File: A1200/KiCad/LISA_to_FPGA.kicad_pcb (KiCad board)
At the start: 2 copper layers, 64 x 37 mm, 28 parts, among them J1 Conn_01x04, J2 Conn_01x40, U1 LM1117-3.3, U2 74LVC162244ADGG, U3 74LVC162244ADGG, U4 LISA, U5 RP2354B

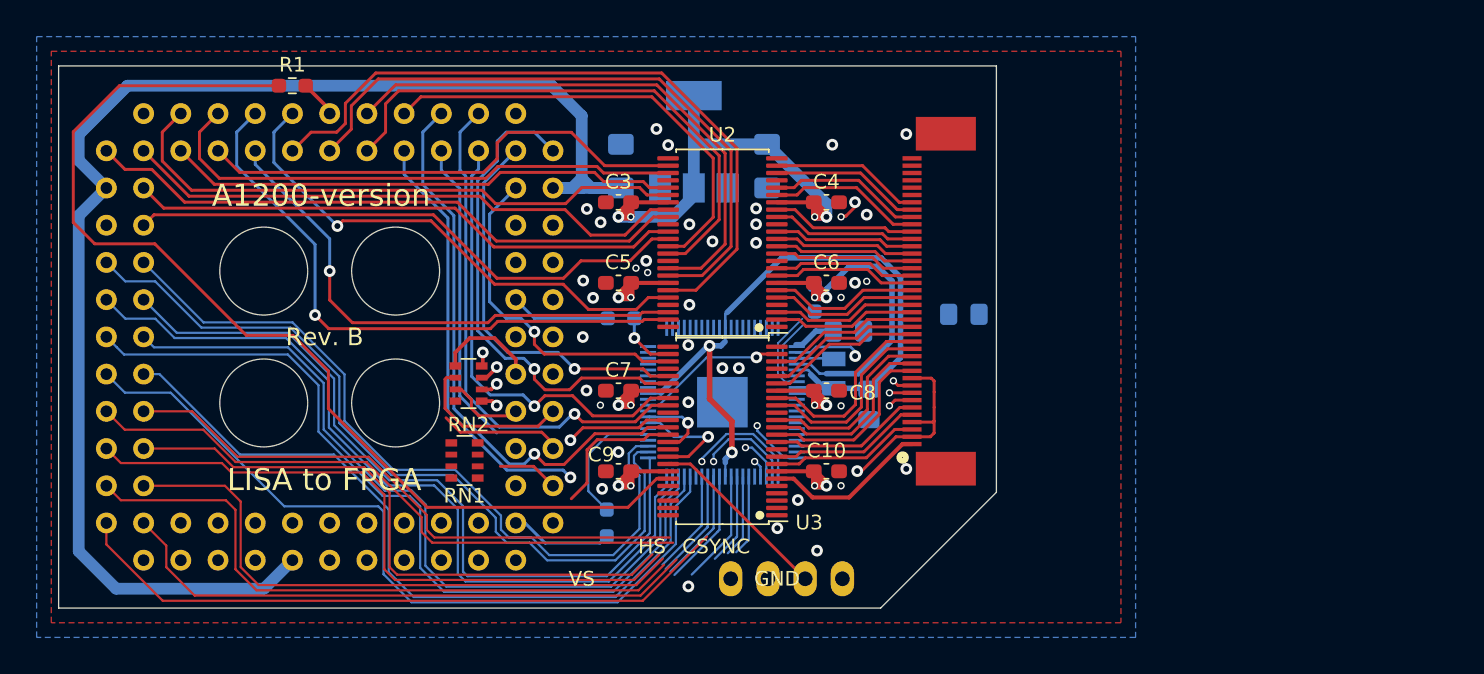
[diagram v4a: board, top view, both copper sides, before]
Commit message: Go to 4 layer and route RGA tracks
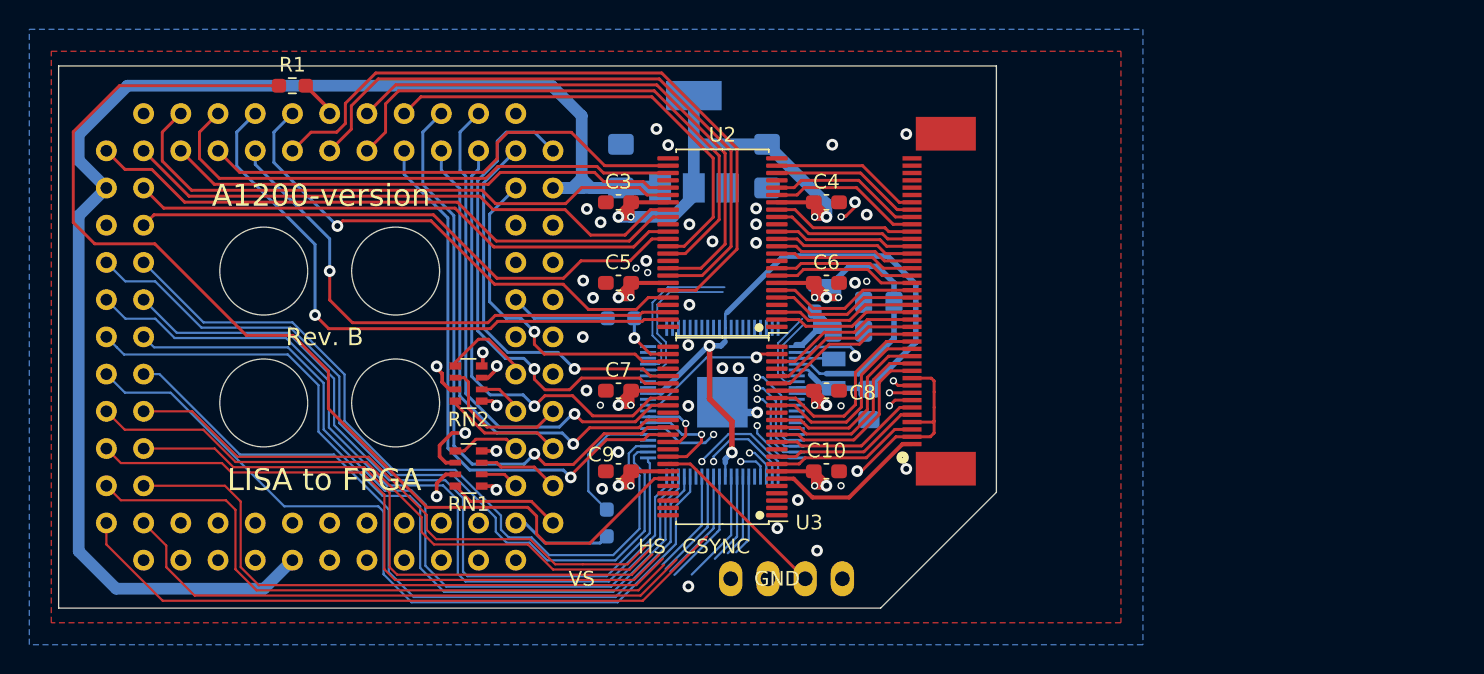
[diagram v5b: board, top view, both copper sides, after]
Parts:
- moved C12 5.86 mm to (204.2, 88.1)
- moved RN1 0.61 mm to (176.2, 99.4), turned to 180 degrees
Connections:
- RN1 pad 2: RGA7 -> /RGA77
- RN1 pad 3: RGA6 -> /RGA66
- RN1 pad 6: /RGA66 -> RGA6
- RN1 pad 7: /RGA77 -> RGA7
- RN2 pad 2: RGA3 -> /RGA33
- RN2 pad 7: /RGA33 -> RGA3
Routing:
- net RGA3: track 1.18 -> 32.2 mm, vias 1 -> 2
- net RGA1: track 0.96 -> 26.7 mm, vias 1 -> 2
- net RGA7: track 2.83 -> 28.4 mm, vias 1 -> 2
- net RGA2: track 1.34 -> 26.1 mm, vias 1 -> 2
- net RGA6: track 6.63 -> 28.6 mm, vias 1 -> 2
- net RGA4: track 4.96 -> 25.2 mm
- net RGA8: track 1.22 -> 21.4 mm, vias 1 -> 2
- net LINK_RET: track 1.70 -> 19.6 mm, vias 1 -> 2
- net RGA5: track 8.01 -> 24.4 mm, vias 1 -> 2
- net RX: track 1.40 -> 12.0 mm
- net TX: track 1.54 -> 12.1 mm
- net 3V3: track 114.2 -> 122.1 mm, vias 17 -> 18
- net /RGA88: track 0.00 -> 7.71 mm
- net /VREG_AVDD: track 2.92 -> 8.55 mm
- net B5: track 28.1 -> 33.5 mm
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- added copper zone on 3V3, net 3V3
- added copper zone on GND, net GND
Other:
- copper layers 2 -> 4

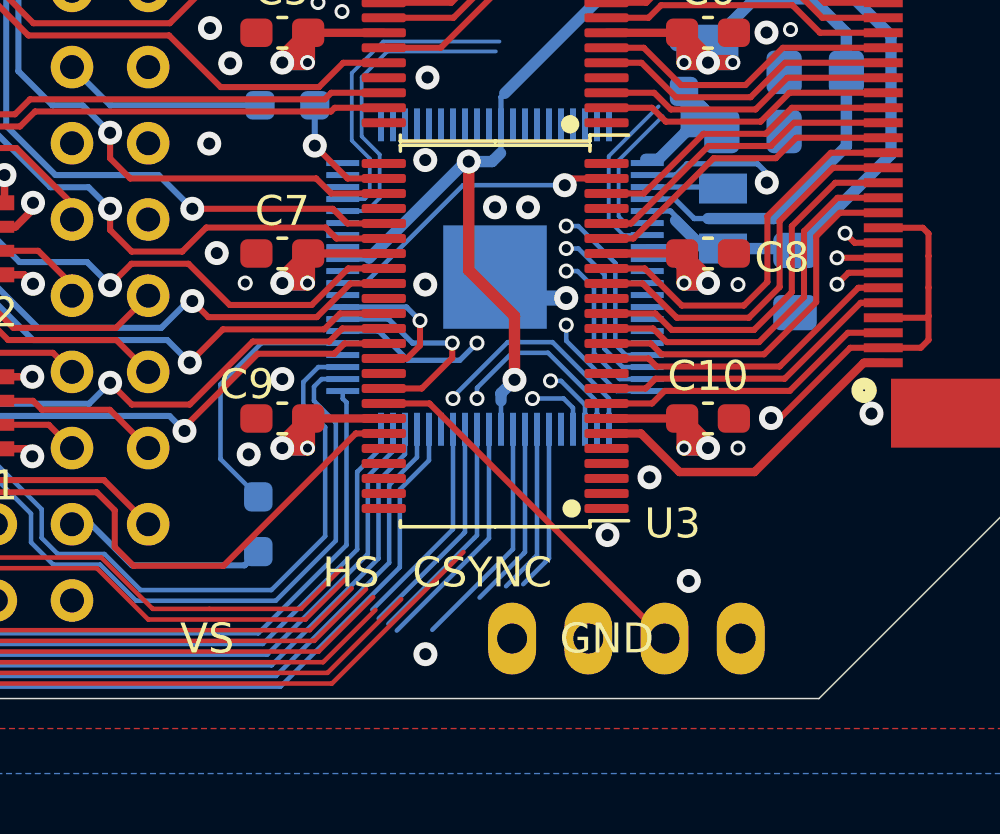
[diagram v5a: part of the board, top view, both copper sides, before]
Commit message: Remove 4-pin header and replace with 1-pin header for Csync only
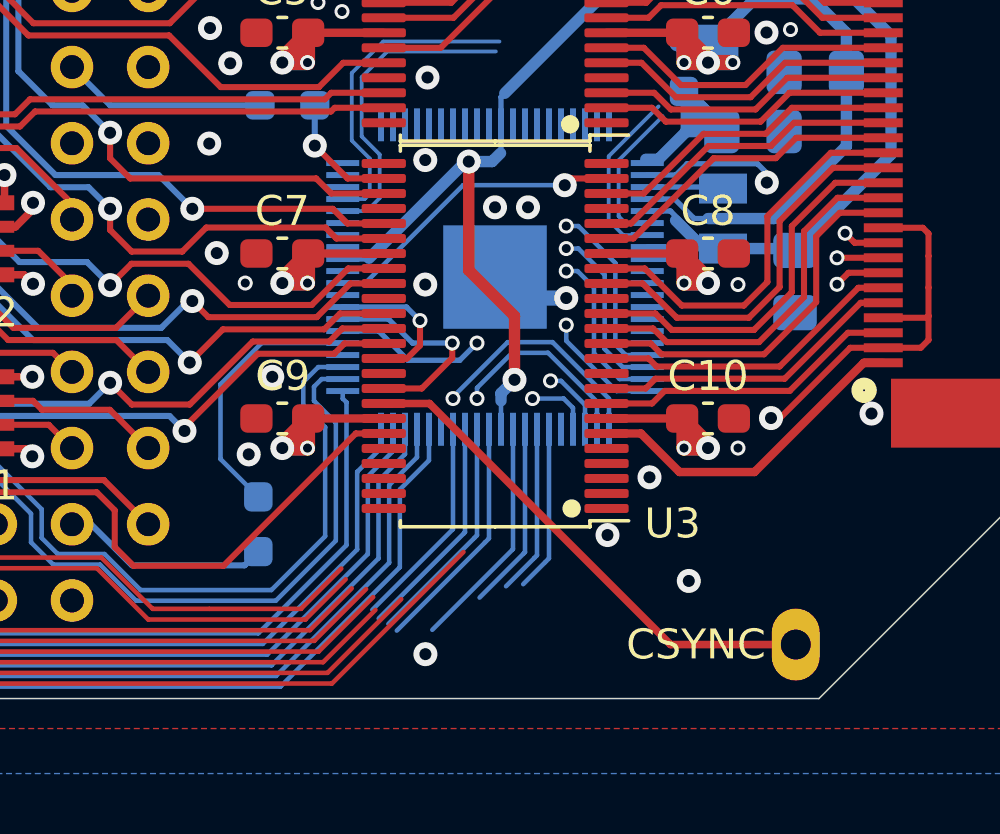
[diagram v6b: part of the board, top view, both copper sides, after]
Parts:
- J1: value Conn_01x04 -> Conn_01x01; footprint Connector_PinHeader_2.54mm:PinHeader_1x04_P2.54mm_Horizontal -> Connector_PinHeader_2.54mm:PinHeader_1x01_P2.54mm_Horizontal
- moved J1 1.85 mm to (203.6, 107.1), turned to 90 degrees
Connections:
- J1 pad 1: GND -> CSYNC
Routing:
- net CSYNC: track 12.9 -> 17.3 mm
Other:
- board text removed: "GND"
- board text removed: "HS"
- board text removed: "HSYNC"
- board text removed: "VS"
- board text removed: "VSYNC"

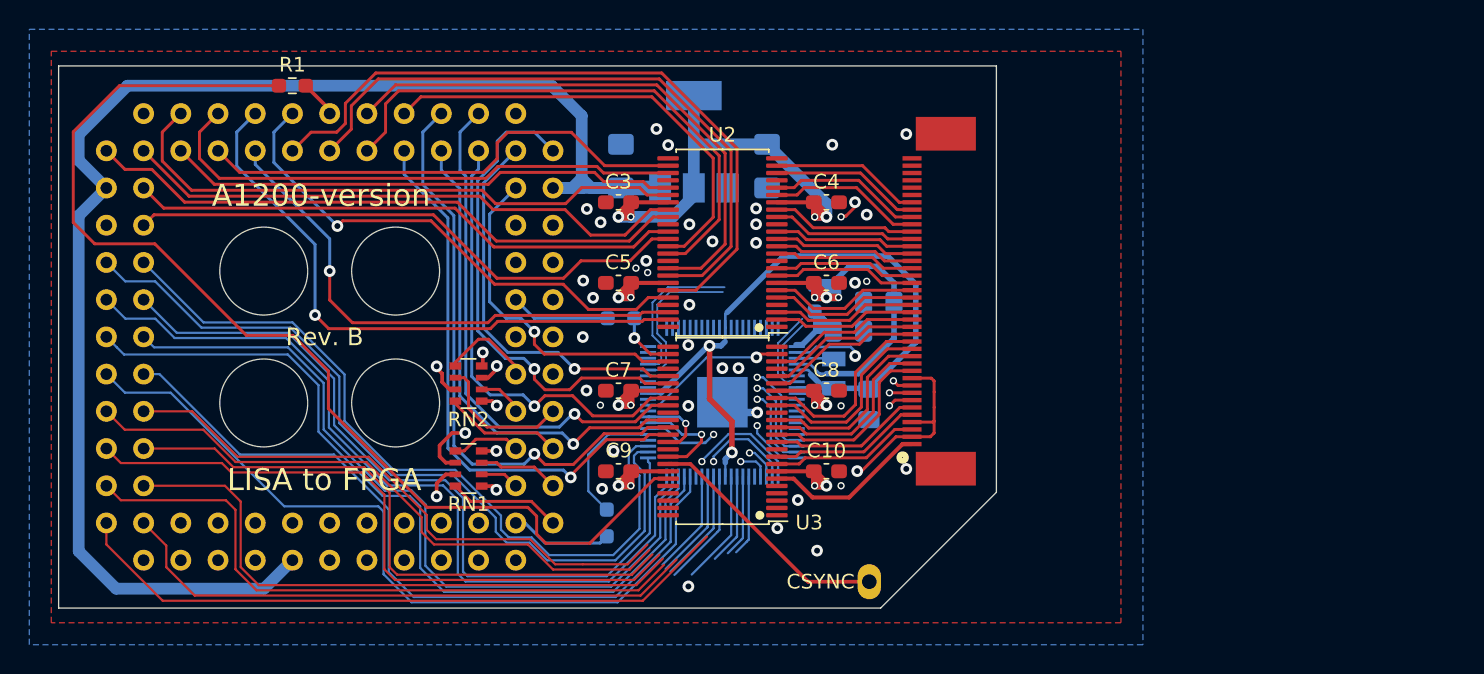
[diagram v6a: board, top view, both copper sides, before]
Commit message: Add 27 Ohm series resistor for the USB signals
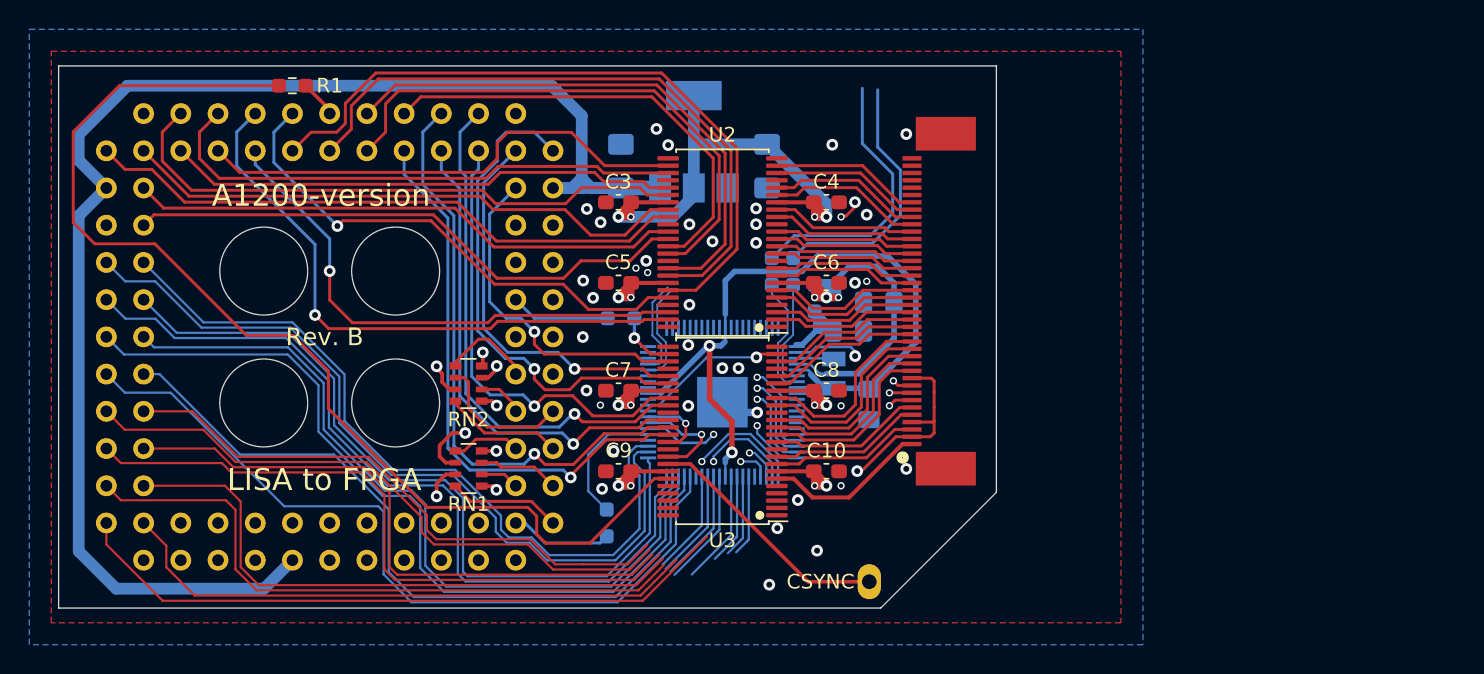
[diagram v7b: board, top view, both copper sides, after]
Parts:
- added R5: 27, Resistor_SMD:R_0603_1608Metric_Pad0.98x0.95mm_HandSolder, B.Cu at (196.9, 86.0)
- added R6: 27, Resistor_SMD:R_0603_1608Metric_Pad0.98x0.95mm_HandSolder, B.Cu at (198.4, 86.0)
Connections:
- U5 pad 66: USB_DM -> Net-(R6-Pad2)
- U5 pad 67: USB_DP -> Net-(R5-Pad2)
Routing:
- net USB_DP: track 5.98 -> 18.9 mm
- net USB_DM: track 4.99 -> 17.7 mm
- net RX: track 12.0 -> 23.4 mm
- net TX: track 12.1 -> 23.4 mm
- net Net-(R5-Pad2): track 0.00 -> 8.33 mm
- net Net-(R6-Pad2): track 0.00 -> 7.33 mm
- net 1V1: track 49.4 -> 50.8 mm
